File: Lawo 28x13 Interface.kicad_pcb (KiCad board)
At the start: 2 copper layers, 83.8 x 48.1 mm, 23 parts, among them IC1 FP2800a, J1 Solder_Jumper, J2 Solder_Jumper, J3 Solder_Jumper, J4 Solder_Jumper, J5 Solder_Jumper, J6 Solder_Jumper, U1 TSR-1

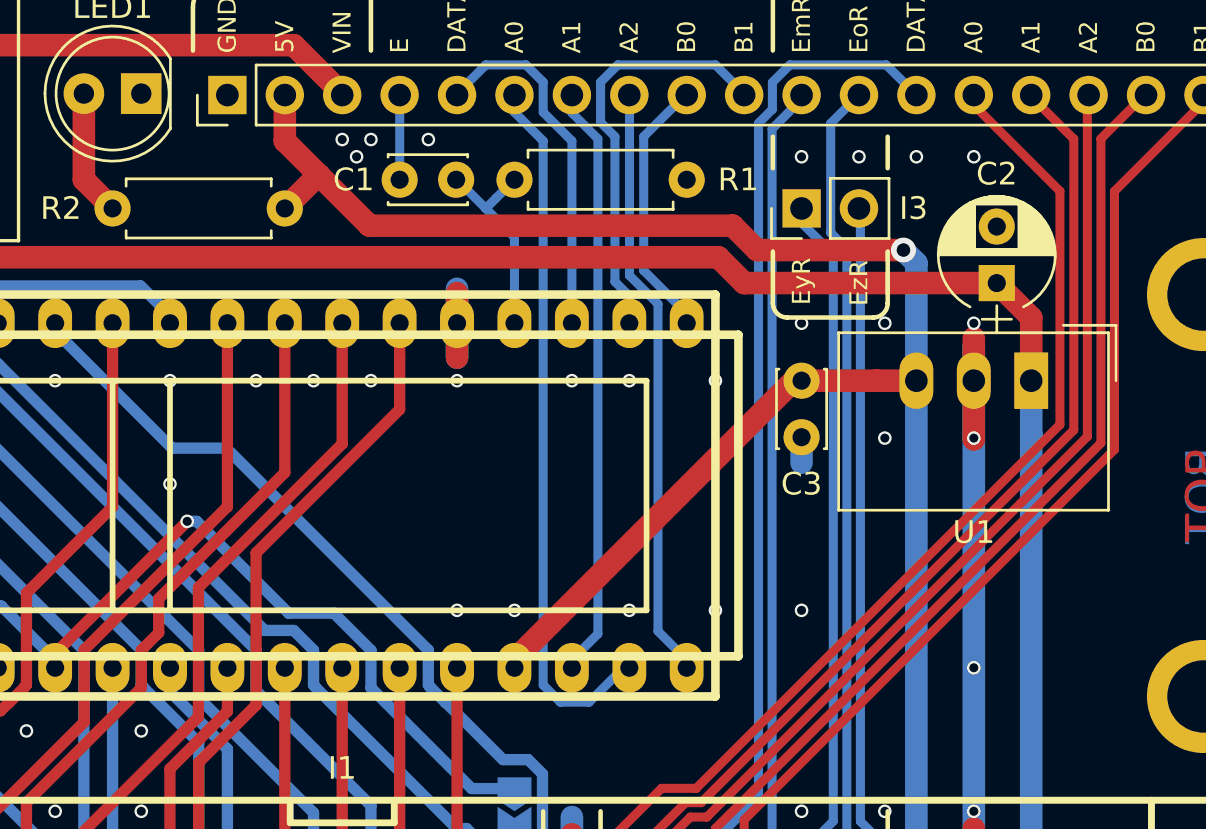
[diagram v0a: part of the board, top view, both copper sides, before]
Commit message: minor PCB updates
- mounting holes are not connected to GND anymore
- one trace and some Vias moved a little bit
- updated/added Silkscreen texts (outlines, parts legend and text related to TSR-1, EyR, and EzR)
- updated plots for the PCB
- new plots for the schematic and PCB images without rendered parts
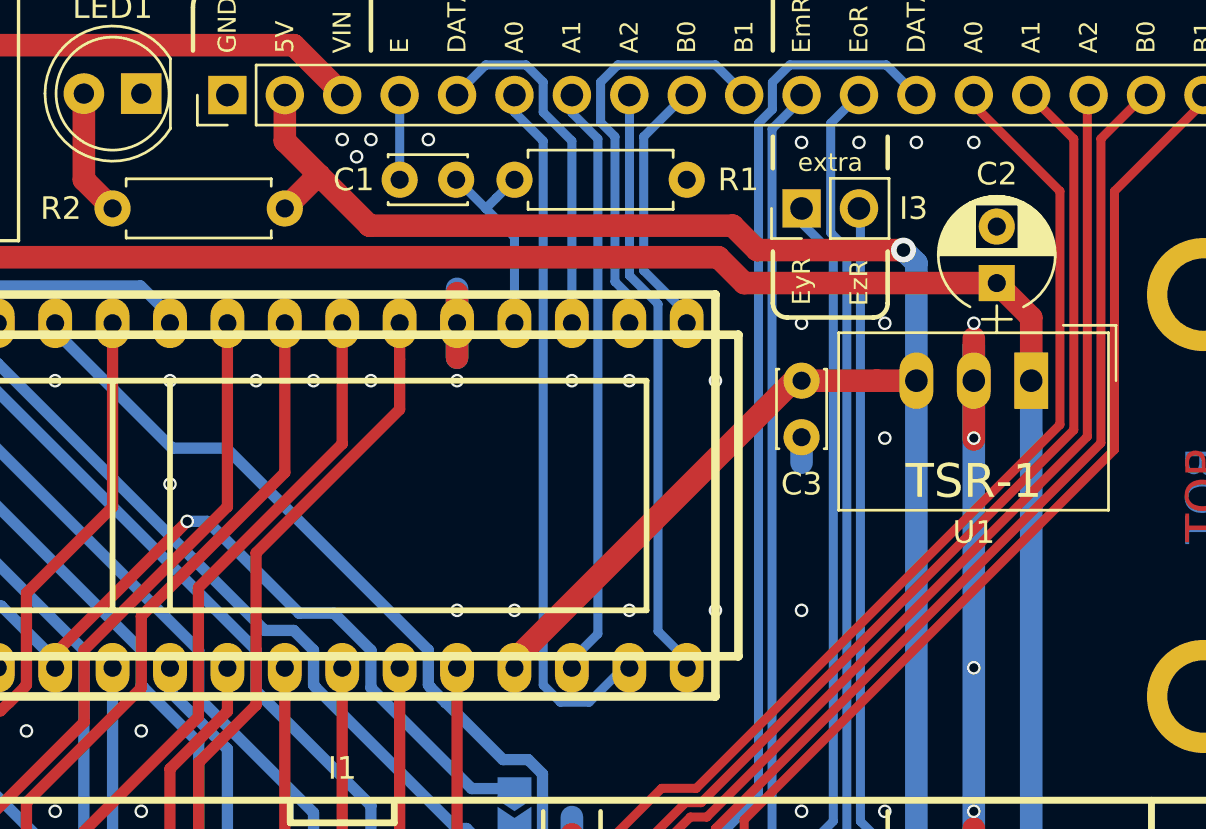
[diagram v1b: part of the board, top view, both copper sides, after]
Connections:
- MTH1 pad 1: GND -> (no net)
- MTH2 pad 1: GND -> (no net)
- MTH3 pad 1: GND -> (no net)
- MTH4 pad 1: GND -> (no net)
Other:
- board text added: "Flip The Dot Lawo 28x13 Interface 1.1.1 April 2019 Robert Römer"
- board text added: "Value 0.22μF 22μF 0.1μF 22k Ω 220 Ω 24V->5V"
- board text added: "extra"
- board text removed: "Flip The Dot Lawo 28x13 Interface 1.1.0 February 2019 Robert Römer"
- board text removed: "Value 0.22μF 22μF 0.1μF 15k 220 24V->5V"

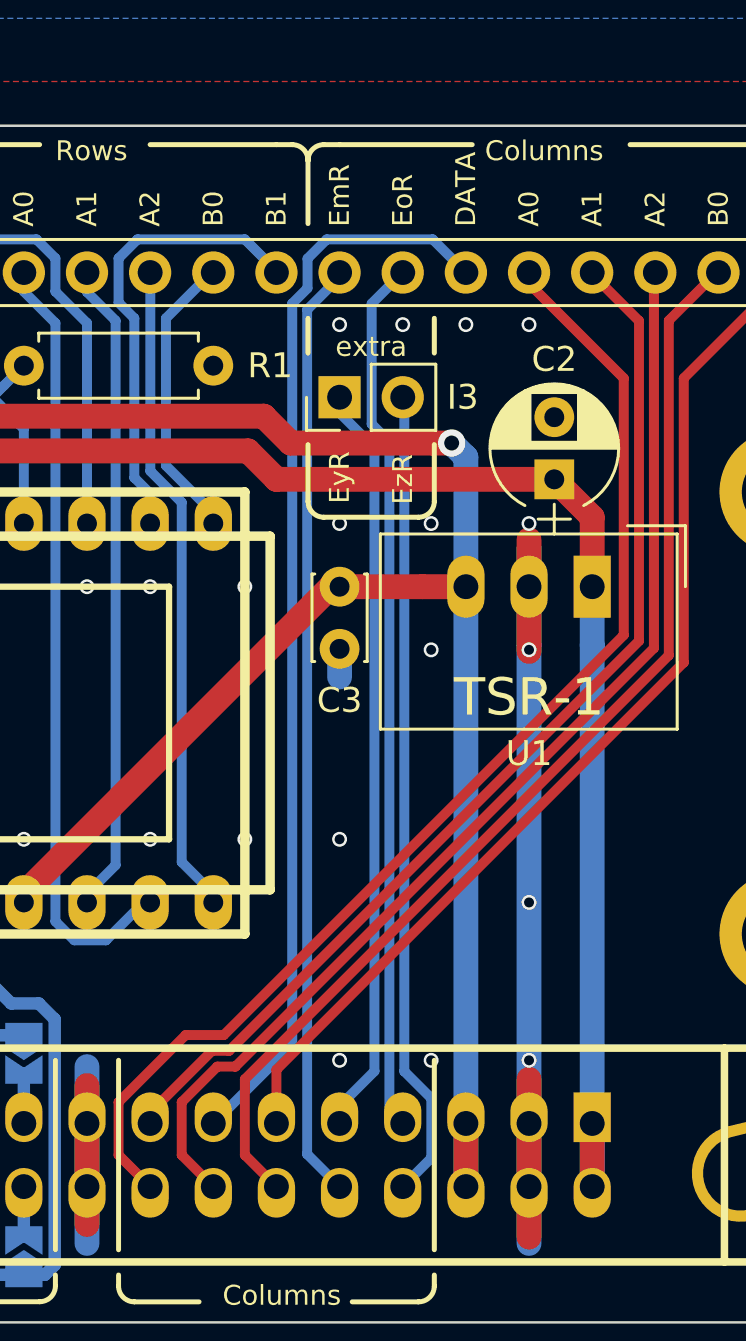
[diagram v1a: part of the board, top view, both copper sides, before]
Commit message: Renamed enable pins and slightly modified traces and silk screen.
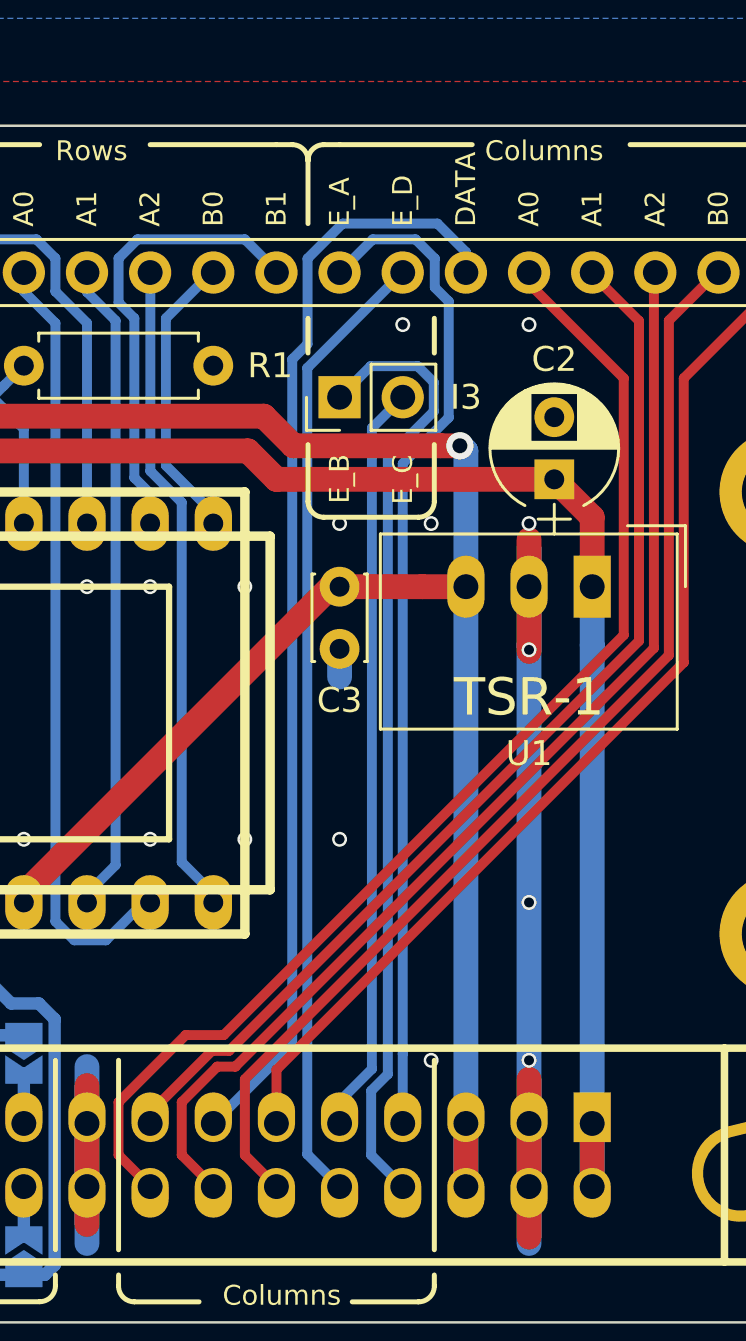
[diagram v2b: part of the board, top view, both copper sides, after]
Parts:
- added ?: Solder_Jumper, Jumper:SolderJumper-2_P1.3mm_Open_TrianglePad1.0x1.5mm, B.Cu at (187.3, 115.5)
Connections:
- I1 pad 10: COL_ENABLE_mR -> COL_ENABLE_D
- I1 pad 7: COL_ENABLE_oR -> COL_ENABLE_A
- I1 pad 8: COL_ENABLE_zR -> COL_ENABLE_B
- I1 pad 9: COL_ENABLE_yR -> COL_ENABLE_C
- I2 pad 11: COL_ENABLE_mR -> COL_ENABLE_A
- I2 pad 12: COL_ENABLE_oR -> COL_ENABLE_D
- I3 pad 1: COL_ENABLE_yR -> COL_ENABLE_B
- I3 pad 2: COL_ENABLE_zR -> COL_ENABLE_C
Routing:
- net COL_ENABLE_A: track 0.00 -> 40.5 mm
- net COL_ENABLE_D: track 0.00 -> 39.1 mm
- net COL_ENABLE_B: track 0.00 -> 38.5 mm
- net COL_ENABLE_mR: track 37.8 -> 0.00 mm
- net COL_ENABLE_oR: track 35.3 -> 0.00 mm
- net COL_ENABLE_zR: track 32.7 -> 0.00 mm
- net COL_ENABLE_yR: track 30.4 -> 0.00 mm
- net COL_ENABLE_C: track 0.00 -> 30.3 mm
- net COL_DATA: track 43.6 -> 44.6 mm
- net GND: vias 51 -> 47
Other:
- board text added: "= EmR = EoR"
- board text added: "Alias E_A E_D"
- board text added: "E_A"
- board text added: "E_B"
- board text added: "E_C"
- board text added: "E_D"
- board text added: "Flip The Dot Lawo Flip Dot 50pin Interface 1.1.2 June 2019 Robert Römer"
- board text added: "Select and bridge one matching pair of jumpers in the „Rows“ box to define and use a 14th row."
- board text removed: "EmR"
- board text removed: "EoR"
- board text removed: "EyR"
- board text removed: "EzR"
- board text removed: "Flip The Dot Lawo 28x13 Interface 1.1.1 April 2019 Robert Römer"
- board text removed: "extra"
